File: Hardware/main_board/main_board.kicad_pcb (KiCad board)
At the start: 2 copper layers, 131.5 x 113 mm, 34 parts

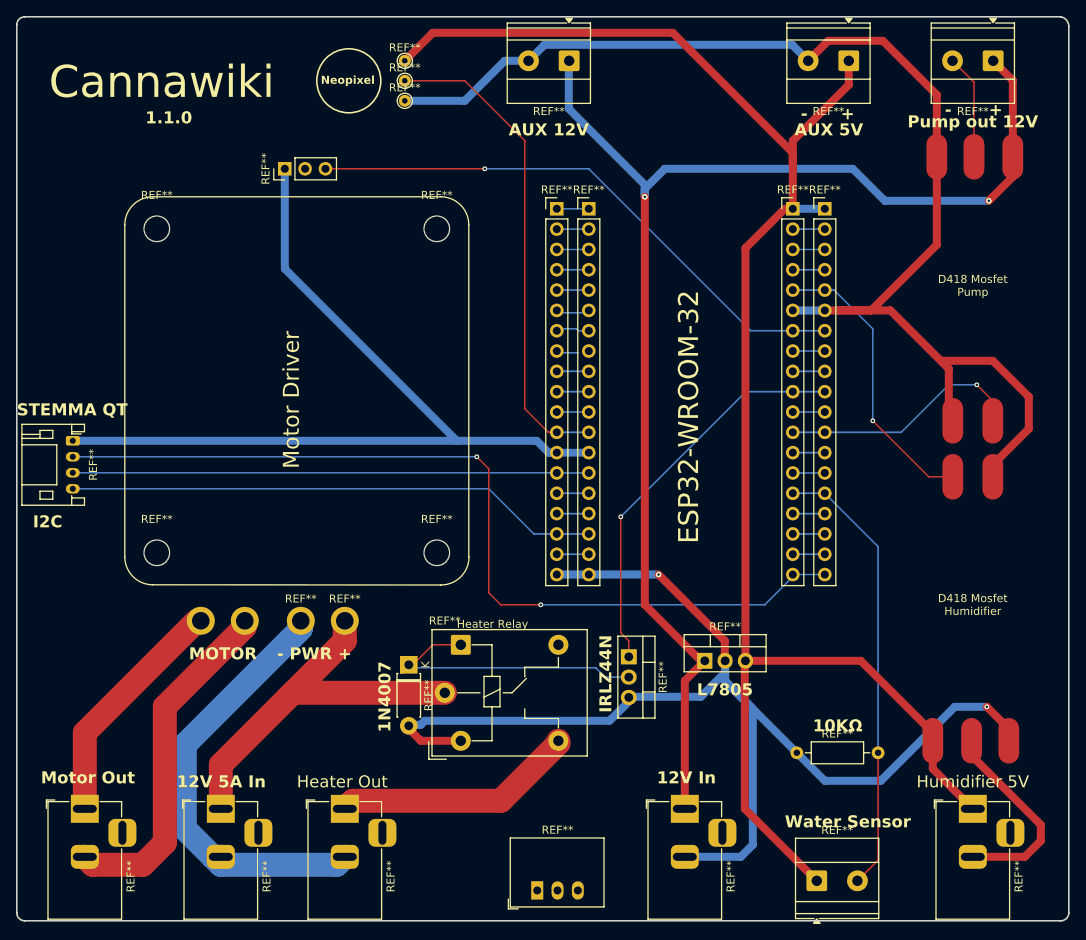
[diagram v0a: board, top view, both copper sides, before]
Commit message: switching power supply
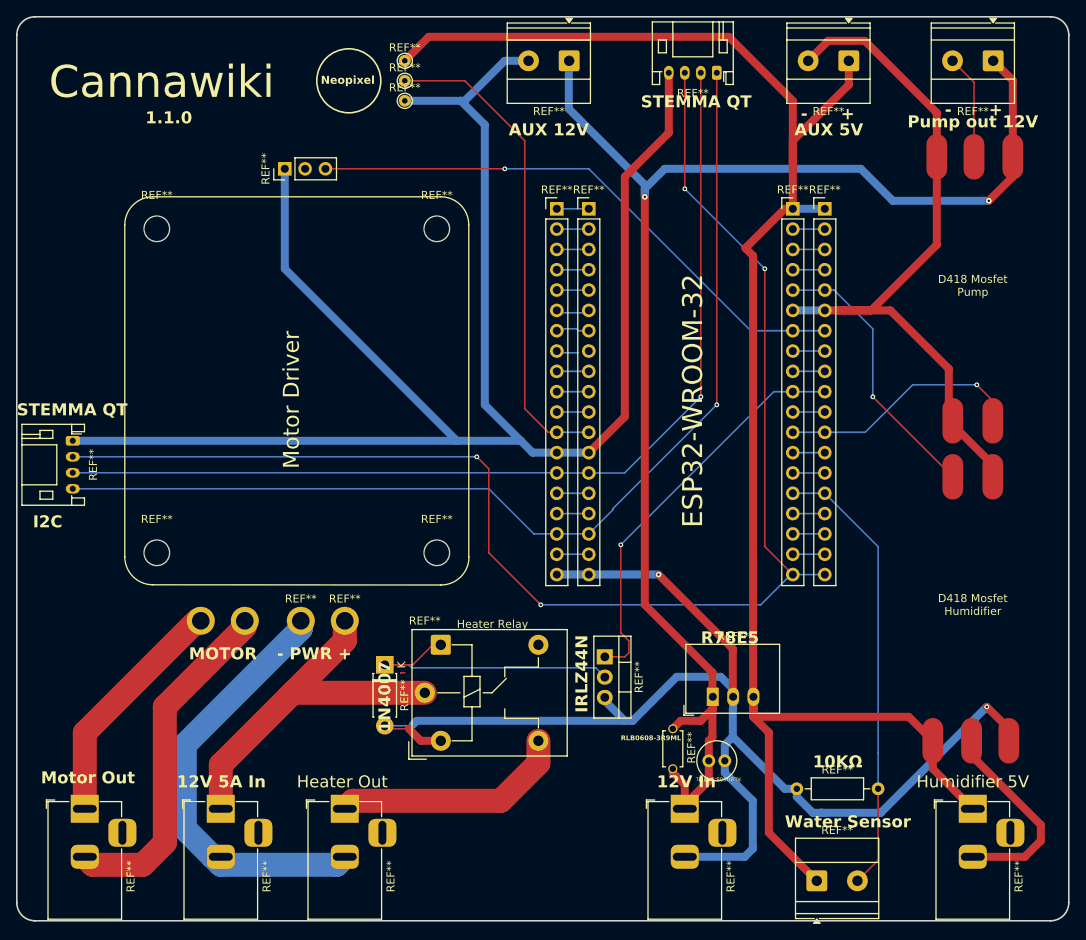
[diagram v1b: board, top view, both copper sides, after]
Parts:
- removed the REF** at (137.5, 119.0)
- added REF**: CAPRB500W50L450T250H550, FK24X7R1C475KR000:CAPRB500W50L450T250H550, F.Cu at (133.5, 130.0)
- added REF**: JST_PH_S4B-PH-K_1x04_P2.00mm_Horizontal, Connector_JST:JST_PH_S4B-PH-K_1x04_P2.00mm_Horizontal, F.Cu at (139.0, 45.5)
- added REF**: RLB0608-3R9ML, Alex_custom:RLB0608-3R9ML, F.Cu at (139.0, 131.5)
- moved REF** 32.7 mm to (138.5, 123.5)
- moved REF** 4.50 mm to (149.0, 135.0)
- moved REF** 3.00 mm to (125.0, 118.5)
- moved REF** 3.00 mm to (97.5, 119.5)
- moved REF** 2.50 mm to (104.5, 117.0)
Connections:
- REF** pad 3V3: (no net) -> 3.3v
- REF** pad 1: (no net) -> 12v+
- REF** pad 2: (no net) -> gnd
- REF** pad 3: (no net) -> 5v+
- REF** pad G21: (no net) -> SDA
- REF** pad G22: (no net) -> SCL
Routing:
- net (no net): track 615.4 -> 371.0 mm, vias 3 -> 1
- net 3.3v: track 0.00 -> 177.7 mm, vias 0 -> 4
- net SCL: track 0.00 -> 131.1 mm, vias 0 -> 1
- net SDA: track 0.00 -> 123.0 mm, vias 0 -> 1
- net gnd: track 434.7 -> 489.3 mm
- net 12v+: track 168.3 -> 180.5 mm
- net Big+: track 48.9 -> 46.4 mm
- net 5v+: track 213.1 -> 215.2 mm
- net humidiferPinOut: track 36.9 -> 35.1 mm
- net HeaterPin: track 49.9 -> 50.5 mm
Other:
- outline, holes or cut-outs redrawn
- board text added: "R78E5"
- board text added: "RLB0608-3R9ML"
- board text removed: "L7805"

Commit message: board 3
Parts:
- removed the REF** at (100.0, 46.5)
- removed the REF** at (100.0, 49.0)
- removed the REF** at (100.0, 44.0)
- removed the REF** at (58.5, 91.5)
- added REF**: LED_WS2812B_PLCC4_5.0x5.0mm_P3.2mm, LED_SMD:LED_WS2812B_PLCC4_5.0x5.0mm_P3.2mm, F.Cu at (93.0, 46.4)
- moved REF** 23.5 mm to (121.0, 120.0)
- moved REF** 15.6 mm to (113.2, 130.0), turned to 180 degrees
- moved REF** 2.55 mm to (139.5, 129.0), turned to 0 degrees
- moved REF** 2.00 mm to (127.0, 118.5)
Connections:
- REF** pad 1: gnd -> (no net)
- REF** pad 2: 12v+ -> (no net)
- REF** pad 14: (no net) -> heaterRelayOut+
- REF** pad A1: (no net) -> heaterTransistorOut
- REF** pad A2: gnd -> 3.3v
- REF** pad 2: (no net) -> heaterTransistorOut
- REF** pad 1: (no net) -> 3.3v
- REF** pad 2: gnd -> heaterTransistorOut
- REF** pad 1: (no net) -> heaterRelayOut+
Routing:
- net gnd: track 489.3 -> 388.1 mm
- net SCL: track 131.1 -> 68.6 mm
- net (no net): track 371.0 -> 310.3 mm
- net SDA: track 123.0 -> 63.3 mm
- net 3.3v: track 177.7 -> 120.3 mm, vias 4 -> 2
- net heaterTransistorOut: track 0.00 -> 26.3 mm
- net heaterRelayOut+: track 0.00 -> 23.0 mm
- net Big+: track 46.4 -> 60.8 mm
- net 5v+: track 215.2 -> 224.1 mm
- net HeaterPin: track 50.5 -> 47.4 mm
- net humidiferGND: track 25.4 -> 24.6 mm
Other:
- board text added: "FK24X7R"
- board text added: "FZ2812-5050"
- board text removed: "I2C"
- board text removed: "RLB0608-3R9ML"

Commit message: Hardware v1.1.1
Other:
- board text added: "1.1.1"
- board text removed: "1.1.0"
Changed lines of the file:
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@@
 		)
 	)
-	(gr_text "1.1.0\n"
+	(gr_text "1.1.1\n"
 		(at 70.5 52 0)
 		(layer "F.SilkS")
